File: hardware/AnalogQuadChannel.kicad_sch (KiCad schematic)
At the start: 14 parts, among them U5 74HC595, U6 SN74LVC126APWR

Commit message: updated Power input on schematic
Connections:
- net DRIVE_CLK renamed SR_CLK
- net DRIVE_LAT renamed SR_LAT
- net DRIVE_OE renamed SR_OE
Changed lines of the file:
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@@
 		)
 	)
-	(hierarchical_label "DRIVE_LAT"
+	(hierarchical_label "SR_LAT"
 		(shape input)
 		(at 53.34 130.81 180)
@@
 		)
 	)
-	(hierarchical_label "DRIVE_OE"
+	(hierarchical_label "SR_OE"
 		(shape input)
 		(at 53.34 133.35 180)
@@
 		)
 	)
-	(hierarchical_label "DRIVE_CLK"
+	(hierarchical_label "SR_CLK"
 		(shape input)
 		(at 53.34 123.19 180)

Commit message: reworked power protection circuit and fixed ERC errors
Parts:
- U7: renamed from U6; footprint Package_SO:SO-14_3.9x8.65mm_P1.27mm -> SN74LVC126APWR:SOP65P640X120-14N
- renumbered C1 to C23, C2 to C24, C3 to C25, C4 to C26, R1 to R11, R2 to R12, R3 to R13, R4 to R14, R5 to R15, R6 to R16, R7 to R17, R8 to R18, U5 to U6

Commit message: added all footprints, updated to 0805, added layout for Jacks
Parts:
- added C49, C53: 100n, Capacitor_SMD:C_0805_2012Metric, symbol Device:C
- C23, C24, C25, C26: footprint Capacitor_SMD:C_0603_1608Metric -> Capacitor_SMD:C_0805_2012Metric
- R11, R12, R13, R14, R15, R16, R17, R18: footprint Resistor_SMD:R_0603_1608Metric -> Resistor_SMD:R_0805_2012Metric
- U7: value SN74LVC126APWR -> SN74LVC126A; footprint SN74LVC126APWR:SOP65P640X120-14N -> SN74LVC126A:SN74LVC126AD; symbol SN74LVC126APWR:SN74LVC126APWR -> SN74LVC126A:SN74LVC126A
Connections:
- net +3.3V: now also C49.1
- net GND: now also C49.2
- net GNDA: now also C53.2
- net VDDA: now also C53.1
- net DRIVE_DI renamed SR_DATA

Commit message: more progress in layout
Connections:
- net at U6.2 (QC): now also U7.4 (2OE); no longer U7.5 (2A)
- net at U6.3 (QD): now also U7.5 (2A); no longer U7.4 (2OE)
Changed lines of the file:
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@@
 	(wire
 		(pts
-			(xy 76.2 123.19) (xy 99.06 123.19)
+			(xy 88.9 123.19) (xy 86.36 125.73)
+		)
+		(stroke
+			(width 0)
+			(type default)
+		)
+	)
+	(wire
+		(pts
+			(xy 86.36 123.19) (xy 88.9 125.73)
 		)
 		(stroke
@@
 	(wire
 		(pts
+			(xy 88.9 125.73) (xy 99.06 125.73)
+		)
+		(stroke
+			(width 0)
+			(type default)
+		)
+	)
+	(wire
+		(pts
 			(xy 248.92 125.73) (xy 248.92 109.22)
 		)
@@
 	(wire
 		(pts
+			(xy 76.2 123.19) (xy 86.36 123.19)
+		)
+		(stroke
+			(width 0)
+			(type default)
+		)
+	)
+	(wire
+		(pts
 			(xy 137.16 143.51) (xy 137.16 146.05)
 		)
@@
 	(wire
 		(pts
+			(xy 99.06 123.19) (xy 88.9 123.19)
+		)
+		(stroke
+			(width 0)
+			(type default)
+		)
+	)
+	(wire
+		(pts
 			(xy 53.34 92.71) (xy 187.96 92.71)
 		)
@@
 	(wire
 		(pts
-			(xy 76.2 125.73) (xy 99.06 125.73)
-		)
-		(stroke
-			(width 0)
-			(type default)
-		)
-	)
-	(wire
-		(pts
 			(xy 53.34 130.81) (xy 55.88 130.81)
 		)
@@
 		)
 		(stroke
+			(width 0)
+			(type default)
+		)
+	)
+	(wire
+		(pts
+			(xy 76.2 125.73) (xy 86.36 125.73)
+		)
+		(stroke

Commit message: schematic updates
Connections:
- net VDDA renamed +2.5V
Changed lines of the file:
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@@
-	)
-	(symbol
-		(lib_id "power:VDDA")
-		(at 137.16 110.49 0)
-		(unit 1)
-		(body_style 1)
-		(exclude_from_sim no)
-		(in_bom yes)
-		(on_board yes)
-		(in_pos_files yes)
-		(dnp no)
-		(fields_autoplaced yes)
-		(property "Reference" "#PWR033"
-			(at 137.16 114.3 0)
-			(hide yes)
-			(show_name no)
-			(do_not_autoplace no)
-			(effects
-				(font
-					(size 1.27 1.27)
-				)
-			)
-		)
-		(property "Value" "VDDA"
-			(at 137.16 105.41 0)
-			(show_name no)
-			(do_not_autoplace no)
-			(effects
-				(font
-					(size 1.27 1.27)
-				)
-			)
-		)
-		(property "Footprint" ""
-			(at 137.16 110.49 0)
-			(hide yes)
-			(show_name no)
-			(do_not_autoplace no)
-			(effects
-				(font
-					(size 1.27 1.27)
-				)
-			)
-		)
-		(property "Datasheet" ""
-			(at 137.16 110.49 0)
-			(hide yes)
-			(show_name no)
-			(do_not_autoplace no)
-			(effects
-				(font
-					(size 1.27 1.27)
-				)
-			)
-		)
-		(property "Description" "Power symbol creates a global label with name \"VDDA\""
-			(at 137.16 110.49 0)
-			(hide yes)
-			(show_name no)
-			(do_not_autoplace no)
-			(effects
-				(font
-					(size 1.27 1.27)
-				)
-			)
-		)
-		(pin "1"
-		)
-		(instances
-			(project "ExpressionController"
-				(path "/acb9d00b-1122-4203-9813-1d558ab77d86/7443422d-b3ef-49a1-9866-4315ff070eb8/00b45eb6-b415-4c04-81c6-325c10c9f99f"
-					(reference "#PWR033")
-					(unit 1)
-				)
-				(path "/acb9d00b-1122-4203-9813-1d558ab77d86/7443422d-b3ef-49a1-9866-4315ff070eb8/335d189b-4e14-4ef9-8d01-ca46b95cd195"
-					(reference "#PWR039")
-					(unit 1)
-				)
-				(path "/acb9d00b-1122-4203-9813-1d558ab77d86/7443422d-b3ef-49a1-9866-4315ff070eb8/e0c025cf-3c12-4b13-8e3c-a9f6b0d8fb23"
-					(reference "#PWR051")
-					(unit 1)
-				)
-				(path "/acb9d00b-1122-4203-9813-1d558ab77d86/7443422d-b3ef-49a1-9866-4315ff070eb8/f05a0872-06f2-4039-9bb0-436624050a93"
-					(reference "#PWR045")
-					(unit 1)
-				)
-			)
-		)
 	)
 	(symbol
@@
 	)
 	(symbol
+		(lib_id "PowerSymbols:+2.5V")
+		(at 152.4 147.32 0)
+		(unit 1)
+		(body_style 1)
+		(exclude_from_sim no)
+		(in_bom yes)
+		(on_board yes)
+		(in_pos_files yes)
+		(dnp no)
+		(fields_autoplaced yes)
+		(property "Reference" "#PWR080"
+			(at 152.4 151.13 0)
+			(hide yes)
+			(show_name no)
+			(do_not_autoplace no)
+			(effects
+				(font
+					(size 1.27 1.27)
+				)
+			)
+		)
+		(property "Value" "+2.5V"
+			(at 152.4 142.24 0)
+			(show_name no)
+			(do_not_autoplace no)
+			(effects
+				(font
+					(size 1.27 1.27)
+				)
+			)
+		)
+		(property "Footprint" ""
+			(at 152.4 147.32 0)
+			(hide yes)
+			(show_name no)
+			(do_not_autoplace no)
+			(effects
+				(font
+					(size 1.27 1.27)
+				)
+			)
+		)
+		(property "Datasheet" ""
+			(at 152.4 147.32 0)
+			(hide yes)
+			(show_name no)
+			(do_not_autoplace no)
+			(effects
+				(font
+					(size 1.27 1.27)
+				)
+			)
+		)
+		(property "Description" "Power symbol creates a global label with name \"+3.3V\""
+			(at 152.4 147.32 0)
+			(hide yes)
+			(show_name no)
+			(do_not_autoplace no)
+			(effects
+				(font
+					(size 1.27 1.27)
+				)
+			)
+		)
+		(pin "1"
+		)
+		(instances
+			(project "ExpressionController"
+				(path "/acb9d00b-1122-4203-9813-1d558ab77d86/7443422d-b3ef-49a1-9866-4315ff070eb8/00b45eb6-b415-4c04-81c6-325c10c9f99f"
+					(reference "#PWR080")
+					(unit 1)
+				)
+				(path "/acb9d00b-1122-4203-9813-1d558ab77d86/7443422d-b3ef-49a1-9866-4315ff070eb8/335d189b-4e14-4ef9-8d01-ca46b95cd195"
+					(reference "#PWR081")
+					(unit 1)
+				)
+				(path "/acb9d00b-1122-4203-9813-1d558ab77d86/7443422d-b3ef-49a1-9866-4315ff070eb8/e0c025cf-3c12-4b13-8e3c-a9f6b0d8fb23"
+					(reference "#PWR097")
+					(unit 1)
+				)
+				(path "/acb9d00b-1122-4203-9813-1d558ab77d86/7443422d-b3ef-49a1-9866-4315ff070eb8/f05a0872-06f2-4039-9bb0-436624050a93"
+					(reference "#PWR096")
+					(unit 1)
+				)
+			)
+		)
+	)
+	(symbol
 		(lib_id "Device:R")
 		(at 175.26 105.41 0)
@@
 	)
 	(symbol
+		(lib_id "PowerSymbols:+2.5V")
+		(at 137.16 110.49 0)
+		(unit 1)
+		(body_style 1)
+		(exclude_from_sim no)
+		(in_bom yes)
+		(on_board yes)
+		(in_pos_files yes)
+		(dnp no)
+		(fields_autoplaced yes)
+		(property "Reference" "#PWR072"
+			(at 137.16 114.3 0)
+			(hide yes)
+			(show_name no)
+			(do_not_autoplace no)
+			(effects
+				(font
+					(size 1.27 1.27)
+				)
+			)
+		)
+		(property "Value" "+2.5V"
+			(at 137.16 105.41 0)
+			(show_name no)
+			(do_not_autoplace no)
+			(effects
+				(font
+					(size 1.27 1.27)
+				)
+			)
+		)
+		(property "Footprint" ""
+			(at 137.16 110.49 0)
+			(hide yes)
+			(show_name no)
+			(do_not_autoplace no)
+			(effects
+				(font
+					(size 1.27 1.27)
+				)
+			)
+		)
+		(property "Datasheet" ""
+			(at 137.16 110.49 0)
+			(hide yes)
+			(show_name no)
+			(do_not_autoplace no)
+			(effects
+				(font
+					(size 1.27 1.27)
+				)
+			)
+		)
+		(property "Description" "Power symbol creates a global label with name \"+3.3V\""
+			(at 137.16 110.49 0)
+			(hide yes)
+			(show_name no)
+			(do_not_autoplace no)
+			(effects
+				(font
+					(size 1.27 1.27)
+				)
+			)
+		)
+		(pin "1"
+		)
+		(instances
+			(project "ExpressionController"
+				(path "/acb9d00b-1122-4203-9813-1d558ab77d86/7443422d-b3ef-49a1-9866-4315ff070eb8/00b45eb6-b415-4c04-81c6-325c10c9f99f"
+					(reference "#PWR072")
+					(unit 1)
+				)
+				(path "/acb9d00b-1122-4203-9813-1d558ab77d86/7443422d-b3ef-49a1-9866-4315ff070eb8/335d189b-4e14-4ef9-8d01-ca46b95cd195"
+					(reference "#PWR073")
+					(unit 1)
+				)
+				(path "/acb9d00b-1122-4203-9813-1d558ab77d86/7443422d-b3ef-49a1-9866-4315ff070eb8/e0c025cf-3c12-4b13-8e3c-a9f6b0d8fb23"
+					(reference "#PWR077")
+					(unit 1)
+				)
+				(path "/acb9d00b-1122-4203-9813-1d558ab77d86/7443422d-b3ef-49a1-9866-4315ff070eb8/f05a0872-06f2-4039-9bb0-436624050a93"
+					(reference "#PWR076")
+					(unit 1)
+				)
+			)
+		)
+	)
+	(symbol
 		(lib_id "Device:C")
 		(at 223.52 105.41 0)
@@
 					(unit 1)
 				)
-			)
-		)
-	)
-	(symbol
-		(lib_id "power:VDDA")
-		(at 152.4 147.32 0)
-		(unit 1)
-		(body_style 1)
-		(exclude_from_sim no)
-		(in_bom yes)
-		(on_board yes)
-		(in_pos_files yes)
-		(dnp no)
-		(fields_autoplaced yes)
-		(property "Reference" "#PWR096"
-			(at 152.4 151.13 0)
-			(hide yes)
-			(show_name no)
-			(do_not_autoplace no)
-			(effects
-				(font
-					(size 1.27 1.27)
-				)
-			)
-		)
-		(property "Value" "VDDA"
-			(at 152.4 142.24 0)
-			(show_name no)
-			(do_not_autoplace no)
-			(effects
-				(font
-					(size 1.27 1.27)
-				)
-			)
-		)
-		(property "Footprint" ""
-			(at 152.4 147.32 0)
-			(hide yes)
-			(show_name no)
-			(do_not_autoplace no)
-			(effects
-				(font
-					(size 1.27 1.27)
-				)
-			)
-		)
-		(property "Datasheet" ""
-			(at 152.4 147.32 0)
-			(hide yes)
-			(show_name no)
-			(do_not_autoplace no)
-			(effects
-				(font
-					(size 1.27 1.27)
-				)
-			)
-		)
-		(property "Description" "Power symbol creates a global label with name \"VDDA\""
-			(at 152.4 147.32 0)
-			(hide yes)
-			(show_name no)
-			(do_not_autoplace no)
-			(effects
-				(font
-					(size 1.27 1.27)
-				)
-			)
-		)
-		(pin "1"
-		)
-		(instances
-			(project "ExpressionController"
-				(path "/acb9d00b-1122-4203-9813-1d558ab77d86/7443422d-b3ef-49a1-9866-4315ff070eb8/00b45eb6-b415-4c04-81c6-325c10c9f99f"
-					(reference "#PWR096")
-					(unit 1)
-				)
-				(path "/acb9d00b-1122-4203-9813-1d558ab77d86/7443422d-b3ef-49a1-9866-4315ff070eb8/335d189b-4e14-4ef9-8d01-ca46b95cd195"
-					(reference "#PWR097")
-					(unit 1)
-				)
-				(path "/acb9d00b-1122-4203-9813-1d558ab77d86/7443422d-b3ef-49a1-9866-4315ff070eb8/e0c025cf-3c12-4b13-8e3c-a9f6b0d8fb23"
-					(reference "#PWR099")
-					(unit 1)
-				)
-				(path "/acb9d00b-1122-4203-9813-1d558ab77d86/7443422d-b3ef-49a1-9866-4315ff070eb8/f05a0872-06f2-4039-9bb0-436624050a93"
-					(reference "#PWR098")
-					(unit 1)
-				)

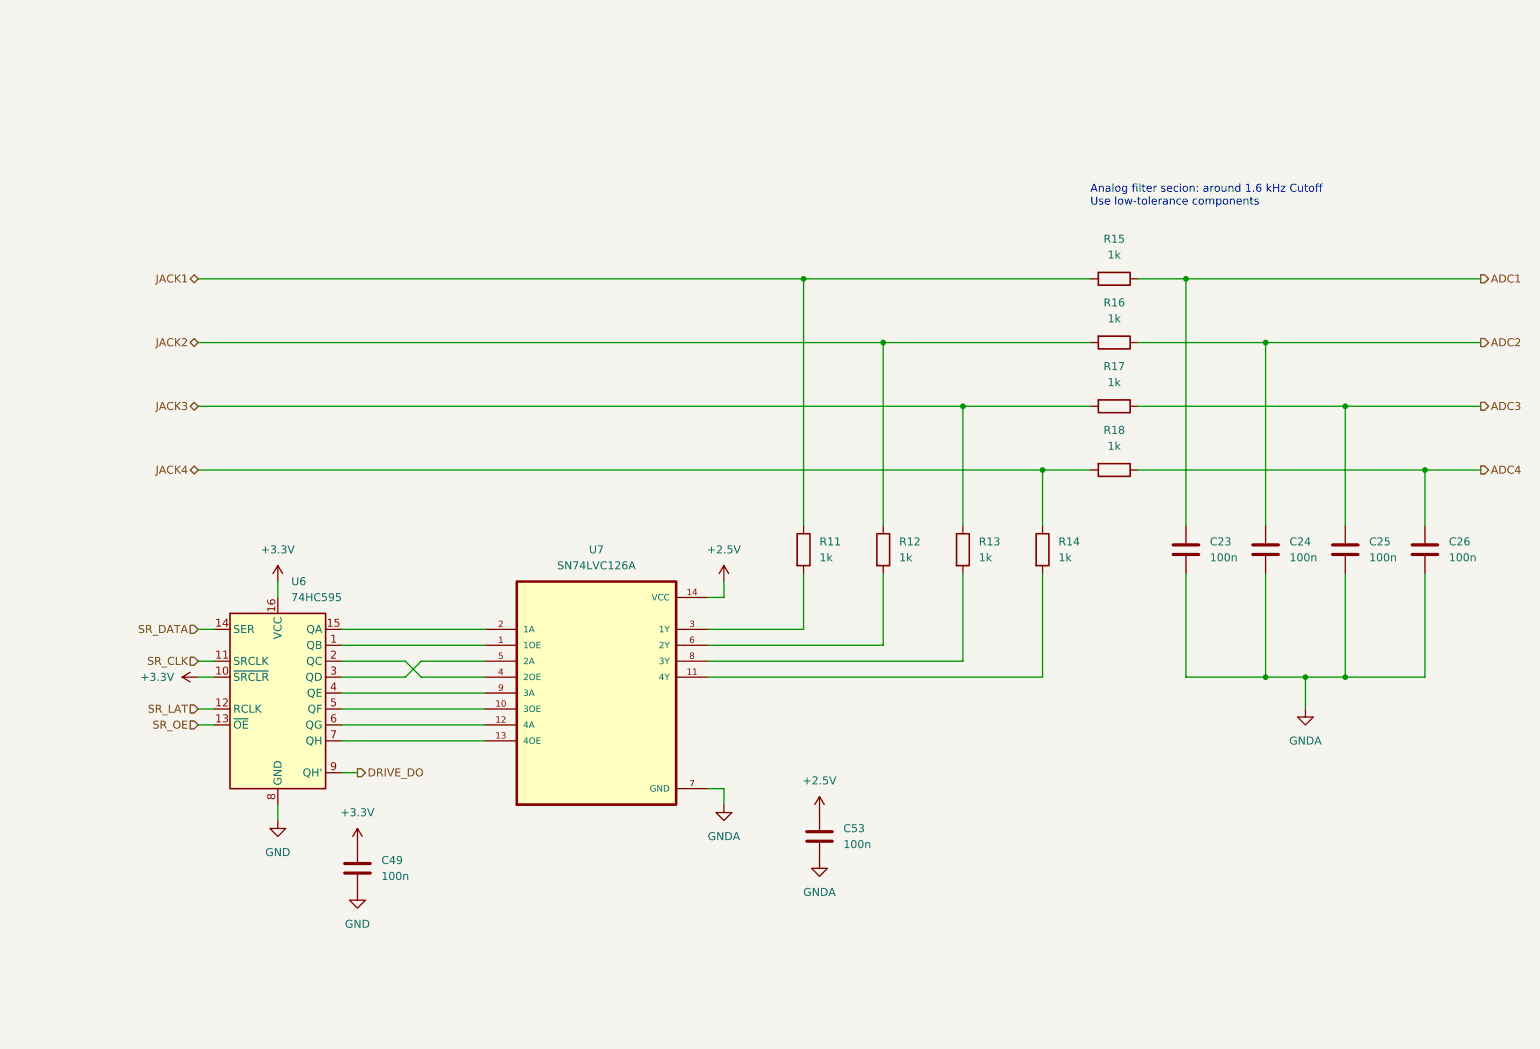
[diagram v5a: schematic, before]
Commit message: replaced buffer ICs with analog switches, schematic bugfixes, started new routing
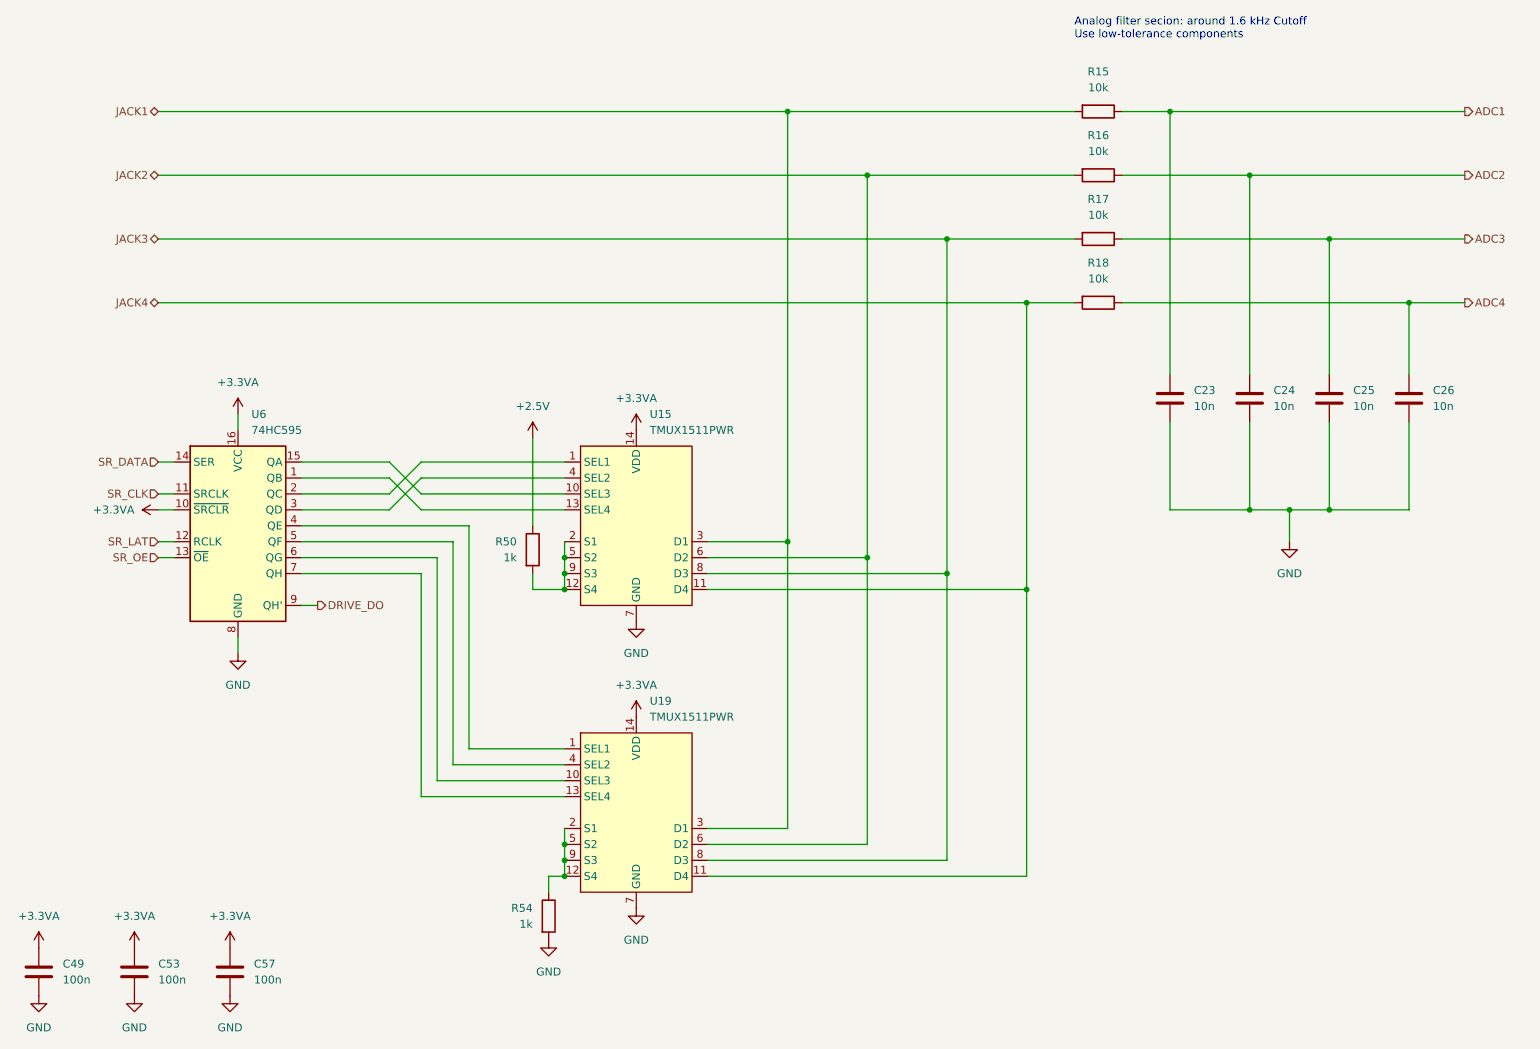
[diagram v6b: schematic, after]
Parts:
- removed R11, R12, R13, R14: 1k, Resistor_SMD:R_0805_2012Metric, symbol Device:R
- removed U7: SN74LVC126A, SN74LVC126A:SN74LVC126AD, symbol SN74LVC126A:SN74LVC126A
- added C57: 100n, Capacitor_SMD:C_0805_2012Metric, symbol Device:C
- added R50, R54: 1k, Resistor_SMD:R_0805_2012Metric, symbol Device:R
- added U15, U19: TMUX1511PWR, Package_SO:TSSOP-14_4.4x5mm_P0.65mm, symbol TMUX1511PWR:TMUX1511PWR
- C23, C24, C25, C26: value 100n -> 10n
- R15, R16, R17, R18: value 1k -> 10k
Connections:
- net GNDA is gone; now on net GND: C23.2, C24.2, C25.2, C26.2, C53.2
- net +2.5V: now also R50.1; no longer C53.1
- net GND: now also C57.2, R54.2, U15.7 (GND), U19.7 (GND)
- net JACK1: now also U15.3 (D1), U19.3 (D1)
- net JACK2: now also U15.6 (D2), U19.6 (D2)
- net JACK3: now also U15.8 (D3), U19.8 (D3)
- net JACK4: now also U15.11 (D4), U19.11 (D4)
- net at U6.1 (QB): now also U15.13 (SEL4)
- net at U6.15 (QA): now also U15.10 (SEL3)
- net at U6.2 (QC): now also U15.1 (SEL1)
- net at U6.3 (QD): now also U15.4 (SEL2)
- net at U6.4 (QE): now also U19.1 (SEL1)
- net at U6.5 (QF): now also U19.4 (SEL2)
- net at U6.6 (QG): now also U19.10 (SEL3)
- net at U6.7 (QH): now also U19.13 (SEL4)
- net +3.3V renamed +3.3VA
- net +3.3VA: now also C53.1, C57.1, U15.14 (VDD), U19.14 (VDD)
- new net: R50.2, U15.12 (S4), U15.2 (S1), U15.5 (S2), U15.9 (S3)
- new net: R54.1, U19.12 (S4), U19.2 (S1), U19.5 (S2), U19.9 (S3)
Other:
- moved on the sheet: C23, C24, C25, C26, C49, C53, R15, R16, R17, R18, U6

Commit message: new PCB updates
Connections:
- net JACK1: now also U15.8 (D3), U19.8 (D3); no longer U15.3 (D1), U19.3 (D1)
- net JACK2: now also U15.11 (D4), U19.11 (D4); no longer U15.6 (D2), U19.6 (D2)
- net JACK3: now also U15.3 (D1), U19.3 (D1); no longer U15.8 (D3), U19.8 (D3)
- net JACK4: now also U15.6 (D2), U19.6 (D2); no longer U15.11 (D4), U19.11 (D4)
- net at U6.1 (QB): now also U15.1 (SEL1); no longer U15.13 (SEL4)
- net at U6.15 (QA): now also U15.4 (SEL2); no longer U15.10 (SEL3)
- net at U6.2 (QC): now also U19.4 (SEL2); no longer U15.1 (SEL1)
- net at U6.3 (QD): now also U19.1 (SEL1); no longer U15.4 (SEL2)
- net at U6.4 (QE): now also U19.13 (SEL4); no longer U19.1 (SEL1)
- net at U6.5 (QF): now also U19.10 (SEL3); no longer U19.4 (SEL2)
- net at U6.6 (QG): now also U15.13 (SEL4); no longer U19.10 (SEL3)
- net at U6.7 (QH): now also U15.10 (SEL3); no longer U19.13 (SEL4)

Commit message: added mouser part numbers
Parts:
- C23, C24, C25, C26, C49, C53, C57, R15, R16, R17, R18: Part Source (none) -> Uni
- R50, R54: value 1k -> 1k 0.1%; Part Source (none) -> Uni/Mouser
- U15, U19: Mouser No (none) -> 595-TMUX1511PWR; Part Source (none) -> Mouser
- U6: value 74HC595 -> 74HC595DR; Mouser No (none) -> 595-SN74HC595DR; Notes (none) -> TODO: swap footprint; Part Source (none) -> Mouser
